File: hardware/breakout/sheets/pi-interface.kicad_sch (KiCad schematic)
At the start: 18 parts, among them J10 Barcode spare 1, J11 Barcode spare 2, J12 Barcode spare 3, J13 Eye camera trigger out (BNC), J14 Behavior camera trigger out 1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, J15 Behavior camera trigger out 2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, J16 Behavior camera trigger out 3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, J17 Behavior camera trigger out 4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, J18 Internal USB-A (sync-module p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, J7 Sync-module 40-pin GPIO heade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, J8 Barcode -> NI optocoupler (Ta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, J9 Barcode -> Intan optocoupler 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, U14 SN74LVC541APW, U15 SN74HCT541PW

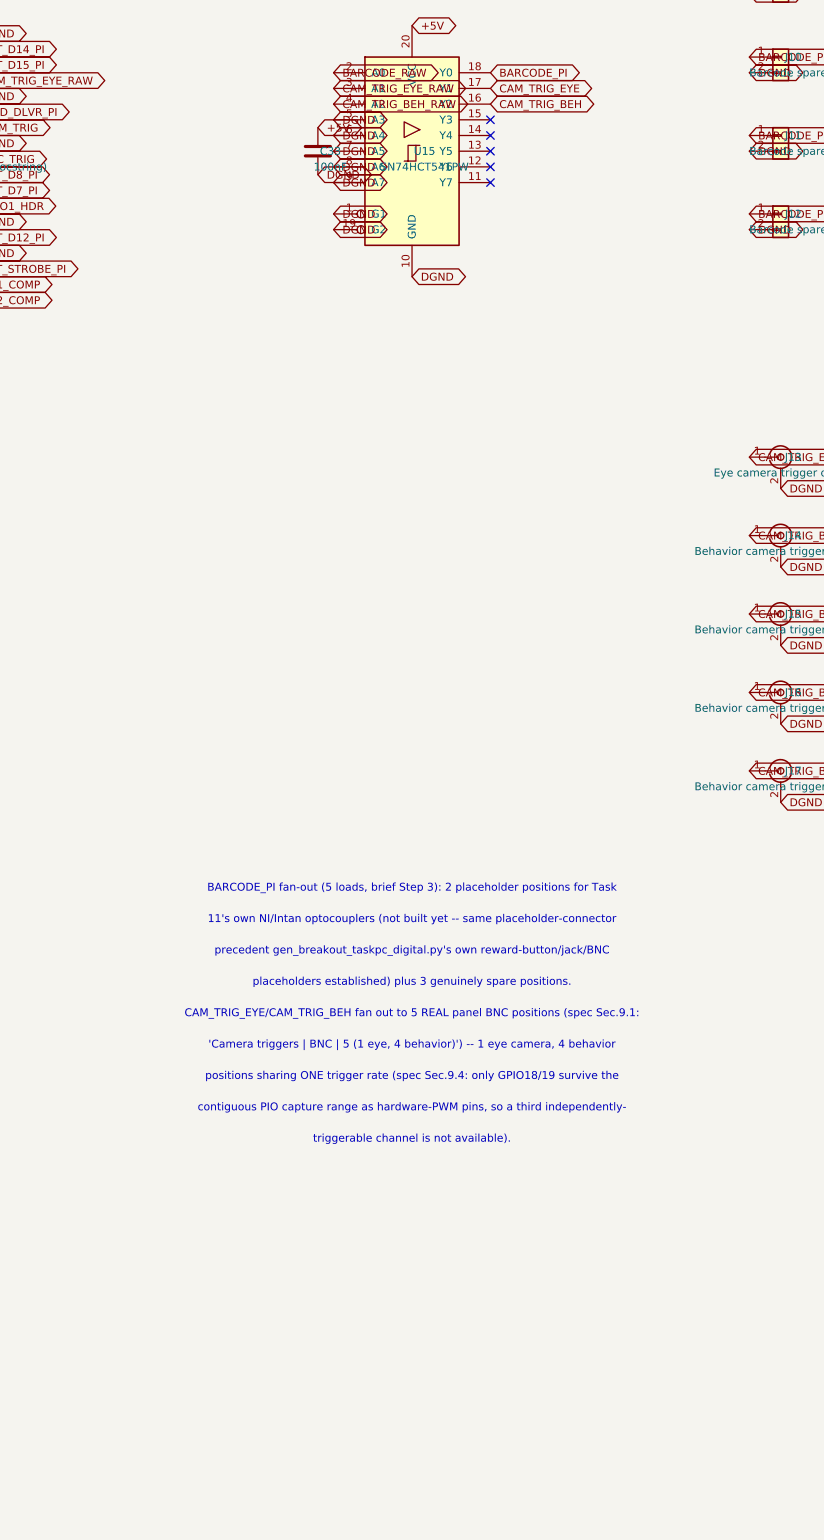
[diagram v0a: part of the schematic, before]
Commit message: fix(hw): one optocoupler LED per driver pin
The _BUF bank names 19 signals for what is really a 30-LED board. The 11
unnamed LEDs got doubled onto pins that already had one, and put +5V on
two sync-module GPIOs.

(a) Doubled loads. Each ACSL-6400/6420 LED draws ~7.33mA from +5V through
430R -- a value pinned between the part's 7-15mA recommended band and its
7.0mA worst-case switching threshold, so it cannot be lowered to suit a
driver. EVT_STROBE_BUF, RWD_CMD_BUF and STIM_TRIG_BUF each fed an NI LED
and an Intan LED from one HCT541 output (14.7mA vs 6mA IOL); BARCODE_PI
did the same off the pi-interface trigger buffer; and bare RWD_DLVR fed
both of its optocouplers straight off the 74HCT32 reward-OR gate, 14.7mA
against 4mA. That last one is the one with a failure mode rather than a
margin: RWD_DLVR's LOW is read by U14 (SN74LVC541APW, V_IL,max 0.8V), and
an HCT gate's VOL at 3.7x its rated sink plausibly exceeds it -- leaving
RWD_DLVR_PI stuck HIGH, the sync module recording reward-delivered
continuously. Same failure signature as the reward-OR polarity defect
caught on this board at task 8 fix round 1.

U10's 5 spare channels now carry EVT_STROBE_INTAN_BUF, RWD_CMD_INTAN_BUF,
STIM_TRIG_INTAN_BUF, RWD_DLVR_BUF and RWD_DLVR_INTAN_BUF (8 of 8 used);
U15's carry BARCODE_BUF and BARCODE_INTAN_BUF. The *_INTAN_BUF legs tap
the same *_CLAMP node their NI twin taps -- the established fan-out
point, one protection network with N buffered copies. RWD_DLVR and
BARCODE_PI now drive only CMOS inputs and panel headers.

(b) +5V reaching GPIO20/21 through an optocoupler LED. R166/R168 (430R
from +5V) fed ACSL-6400 LEDs whose cathodes sat on PD1_COMP/PD2_COMP --
which wire DIRECTLY into the sync module's GPIO20/21. With the LED off
that node idles ~3.6-3.8V, above the 3.3V rail and held only by the
module's ESD clamp; with this board powered and the sync box off, ~7mA is
injected into an unpowered pad. These were the only 2 of 24 NI
optocoupler LEDs not driven from a buffered le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
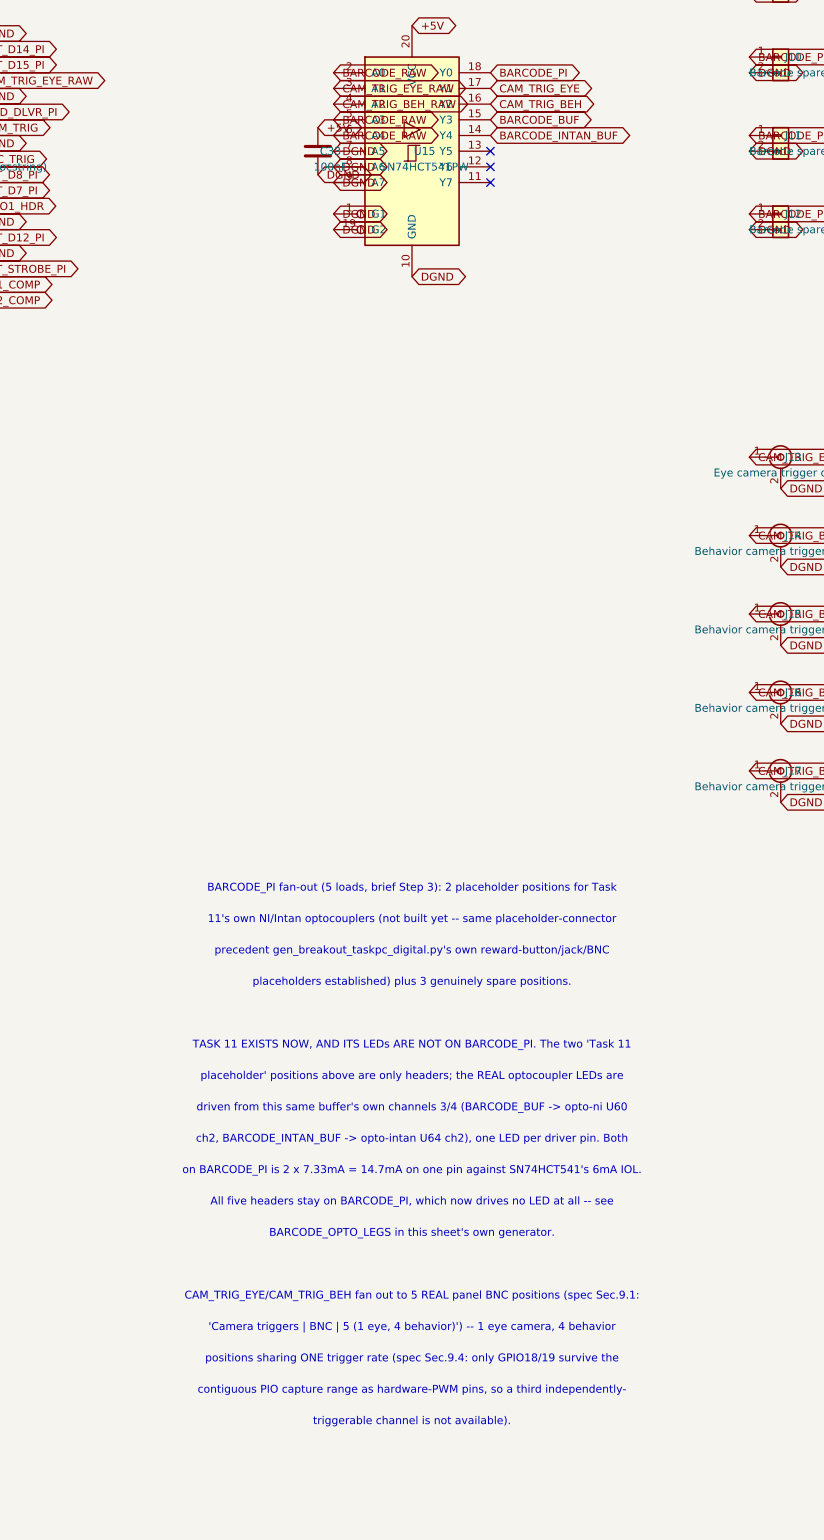
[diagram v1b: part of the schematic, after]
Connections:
- net BARCODE_RAW: now also U15.5 (A3), U15.6 (A4)
- net DGND: no longer U15.5 (A3), U15.6 (A4)
- net BARCODE_INTAN_BUF: now reaches U15.14 (Y4)
- net BARCODE_BUF: now reaches U15.15 (Y3)
- no-connect marks 18 -> 16
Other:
- note added: "All five headers stay on BARCODE_PI, which now drives no LED at all -- see"
- note added: "BARCODE_OPTO_LEGS in this sheet's own generator."
- note added: "TASK 11 EXISTS NOW, AND ITS LEDs ARE NOT ON BARCODE_PI. The two 'Task 11"
- note added: "ch2, BARCODE_INTAN_BUF -> opto-intan U64 ch2), one LED per driver pin. Both"
- note added: "driven from this same buffer's own channels 3/4 (BARCODE_BUF -> opto-ni U60"
- note added: "on BARCODE_PI is 2 x 7.33mA = 14.7mA on one pin against SN74HCT541's 6mA IOL."
- note added: "placeholder' positions above are only headers; the REAL optocoupler LEDs are"

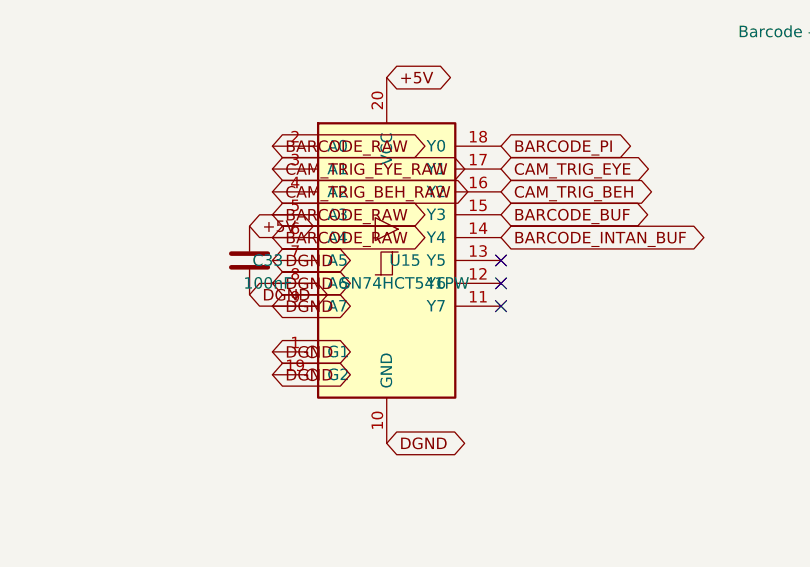
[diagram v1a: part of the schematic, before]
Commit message: fix(hw): swap SN74AHCT541PW in for SN74HCT541PW on U8-U11, U15
Each of these five packages drives exactly one ACSL-6400/6420 LED at
~7.33mA, fixed by the LED's own 7.0mA worst-case switching threshold,
not a driver choice. SN74HCT541PW is rated IOL=6mA: 7.33mA is 22% over
the rated sink -- far inside the part's 25mA per-pin absolute maximum,
but past its guaranteed-VOL condition, and the prior report's own
"22% over, bounded" framing was self-inconsistent: it applied the
datasheet VOL figure quoted at the rated 6mA to a 7.33mA load. Solved
self-consistently against the part's own ~55 ohm output impedance (not
the single 6mA test point), the real current is closer to 7.18mA --
uncomfortably close to the LED's own 7.0mA floor, and below it at V_F
max with the 5V rail 5% low. Running out of spec was eroding exactly
the margin the out-of-spec operation was meant to buy.

SN74AHCT541PW is rated IOL=8mA (identical pinout, identical TSSOP-20
footprint, same 74xx:74LS541-derived KiCad symbol family), making
7.33mA fully compliant with margin, and doubles both absolute maxima
(25mA->50mA/pin, 70mA->100mA/package) -- retiring the separate concern
that U8/U9/U10 sat at 58.6mA of a 70mA package limit.

Confirmed to be exactly what it should be: a Value/MPN edit on five
refdes, zero refdes churn, no footprint change. Diffing the whole
board's own component list (netlist-contract.json) against the prior
commit shows only U8/U9/U10/U11/U15 changing Value, nothing else added,
removed, or renumbered.

check_taskpc_digital_netlist.py and check_breakout_pi_interface_netlist.py
updated to expect the new Value on these exact five references (both
files independently redefine their own contract rather than importing
the generator's, so both needed the literal string updated); the "one
LED per driver pin" invariant they enforce is unaffected -- doubling up
would still overload the new part's own 8mA rating just as surely.

AHCT's faster edges are a layout-stage concern, not a schematic-ca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
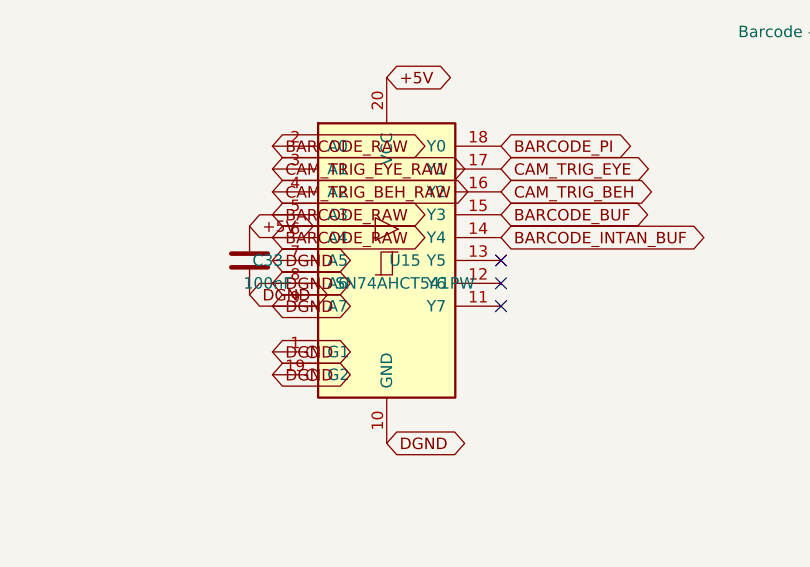
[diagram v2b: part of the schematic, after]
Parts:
- removed U15: SN74HCT541PW, Package_SO:Texas_PW0020A_TSSOP-20_4.4x6.5mm_P0.65mm, symbol 74xx:74HCT541
- added U15: SN74AHCT541PW, Package_SO:Texas_PW0020A_TSSOP-20_4.4x6.5mm_P0.65mm, symbol 74xx:74AHCT541
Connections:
- net +5V: now also U15.20 (VCC)
- net BARCODE_BUF: now also U15.15 (Y3)
- net BARCODE_INTAN_BUF: now also U15.14 (Y4)
- net BARCODE_PI: now also U15.18 (Y0)
- net BARCODE_RAW: now also U15.2 (A0), U15.5 (A3), U15.6 (A4)
- net CAM_TRIG_BEH: now also U15.16 (Y2)
- net CAM_TRIG_BEH_RAW: now also U15.4 (A2)
- net CAM_TRIG_EYE: now also U15.17 (Y1)
- net CAM_TRIG_EYE_RAW: now also U15.3 (A1)
- net DGND: now also U15.1 (G1), U15.10 (GND), U15.19 (G2), U15.7 (A5), U15.8 (A6), U15.9 (A7)
